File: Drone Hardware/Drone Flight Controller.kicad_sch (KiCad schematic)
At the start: 51 parts, among them J1 USB_B_Micro, J10 UART6_RX, J11 SDA_PAD, J12 PPM_IN, J13 UART3_TX, J14 UART3_RX, J15 Pad, J2 S4, J3 S1, J4 UART1_TX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

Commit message: Basic PCB outline created
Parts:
- SW1: footprint (none) -> Button_Switch_SMD:SW_DIP_SPSTx01_Slide_Copal_CVS-01xB_W5.9mm_P1mm
- Y1: footprint (none) -> Crystal:Crystal_SMD_3225-4Pin_3.2x2.5mm
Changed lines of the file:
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@@
     (property "Reference" "Y1" (id 0) (at 148.59 80.01 0))
     (property "Value" "8MHz" (id 1) (at 149.86 90.17 0))
-    (property "Footprint" "" (id 2) (at 146.05 85.09 0)
+    (property "Footprint" "Crystal:Crystal_SMD_3225-4Pin_3.2x2.5mm" (id 2) (at 146.05 85.09 0)
       (effects (font (size 1.27 1.27)) hide)
     )
@@
     (property "Reference" "SW1" (id 0) (at 148.59 54.61 0))
     (property "Value" "SW_SPDT" (id 1) (at 148.59 62.23 0))
-    (property "Footprint" "" (id 2) (at 147.32 57.15 0)
+    (property "Footprint" "Button_Switch_SMD:SW_DIP_SPSTx01_Slide_Copal_CVS-01xB_W5.9mm_P1mm" (id 2) (at 147.32 57.15 0)
       (effects (font (size 1.27 1.27)) hide)
     )
@@
     )
     (path "/f7f7def0-4a30-49f0-a6ee-43201f0a01bb"
-      (reference "SW1") (unit 1) (value "SW_SPDT") (footprint "")
+      (reference "SW1") (unit 1) (value "SW_SPDT") (footprint "Button_Switch_SMD:SW_DIP_SPSTx01_Slide_Copal_CVS-01xB_W5.9mm_P1mm")
     )
     (path "/da8d870f-60bd-4388-b575-5bfb17f73489"
@@
     )
     (path "/d088e369-8987-468f-b0cd-47a0a3df6e73"
-      (reference "Y1") (unit 1) (value "8MHz") (footprint "")
-    )
-  )
+      (reference "Y1") (unit 1) (value "8MHz") (footprint "Crystal:Crystal_SMD_3225-4Pin_3.2x2.5mm")
+    )
+  )

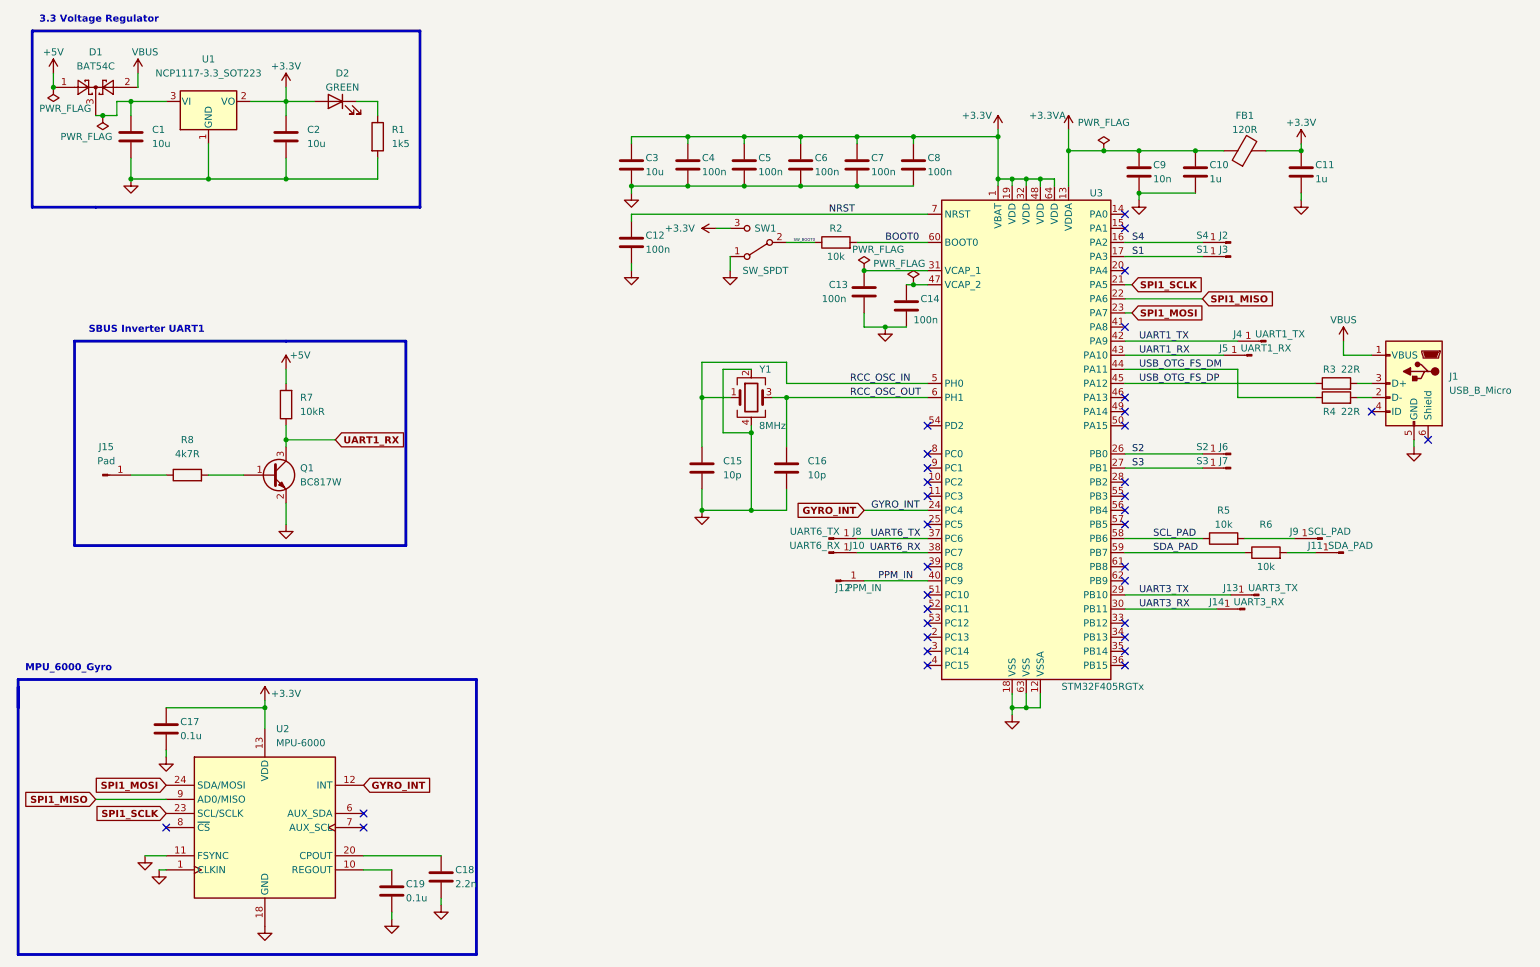
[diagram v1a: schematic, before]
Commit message: Wired the decoupling capacitors, crystal and USB
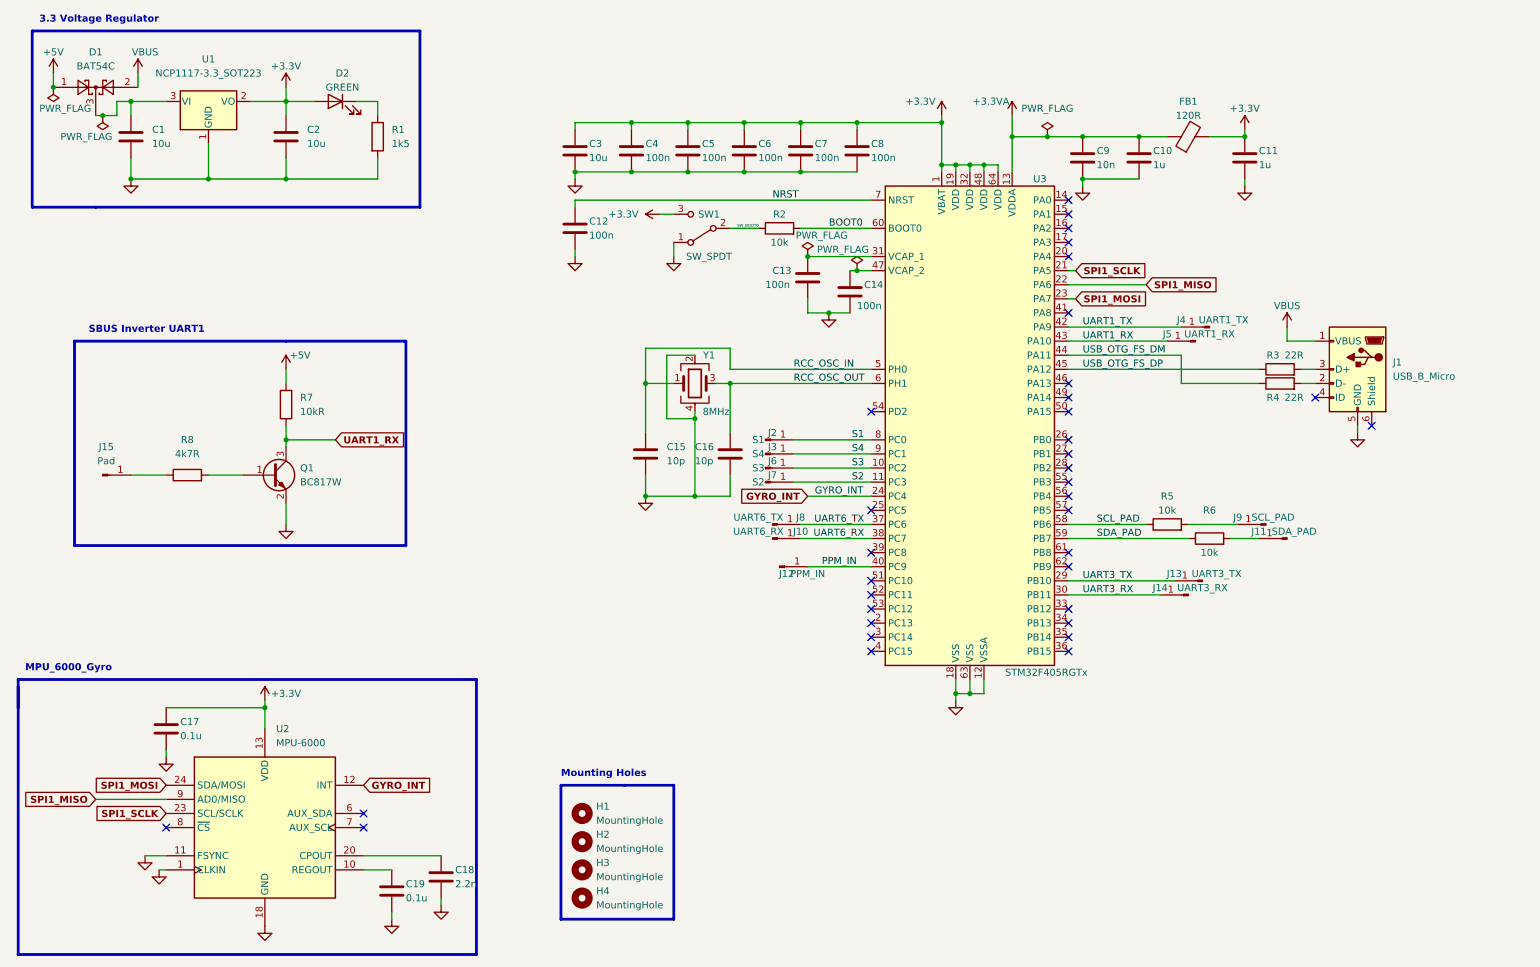
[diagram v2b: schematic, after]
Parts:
- added H1, H2, H3, H4: MountingHole, MountingHole:MountingHole_2.2mm_M2, symbol Mechanical:MountingHole
- J2: value S4 -> S1; footprint Connector_Wire:SolderWirePad_1x01_SMD_5x10mm -> Connector_Wire:SolderWirePad_1x01_SMD_1x2mm
- J3: value S1 -> S4; footprint Connector_Wire:SolderWirePad_1x01_SMD_5x10mm -> Connector_Wire:SolderWirePad_1x01_SMD_1x2mm
- J6: value S2 -> S3; footprint Connector_Wire:SolderWirePad_1x01_SMD_5x10mm -> Connector_Wire:SolderWirePad_1x01_SMD_1x2mm
- J7: value S3 -> S2; footprint Connector_Wire:SolderWirePad_1x01_SMD_5x10mm -> Connector_Wire:SolderWirePad_1x01_SMD_1x2mm
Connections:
- net S1: now also J2.1 (Pin_1), U3.8 (PC0); no longer J3.1 (Pin_1), U3.17 (PA3)
- net S2: now also J7.1 (Pin_1), U3.11 (PC3); no longer J6.1 (Pin_1), U3.26 (PB0)
- net S3: now also J6.1 (Pin_1), U3.10 (PC2); no longer J7.1 (Pin_1), U3.27 (PB1)
- net S4: now also J3.1 (Pin_1), U3.9 (PC1); no longer J2.1 (Pin_1), U3.16 (PA2)
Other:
- note added: "Mounting Holes"
- moved on the sheet: C10, C11, C12, C13, C14, C15, C16, C3, C4, C5, C6, C7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

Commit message: Reconfigured linux repository and finished version 1.0 of the flight controller.
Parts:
- removed J15: Pad, Connector_Wire:SolderWirePad_1x01_SMD_1x2mm, symbol Connector:Conn_01x01_Male
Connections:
- net +5V: now also C1.1, D1.3, U1.3 (VI); no longer D1.1
- net at R8.1: now also J5.1 (Pin_1)
- net UART1_RX renamed UART1_RX_OUT
- net UART1_RX_OUT: no longer J5.1 (Pin_1)
- new net VDD: D1.1
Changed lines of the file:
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@@
   (junction (at 62.23 92.71) (diameter 0) (color 0 0 0 0)
+  )
+  (junction (at 27.94 34.29) (diameter 0) (color 0 0 0 0)
   )
   (junction (at 124.46 35.56) (diameter 0) (color 0 0 0 0)
@@
     (stroke (width 0) (type default) (color 0 0 0 0))
   )
+  (wire (pts (xy 20.32 35.56) (xy 27.94 35.56))
+    (stroke (width 0) (type default) (color 0 0 0 0))
+  )
   (wire (pts (xy 185.42 43.18) (xy 185.42 44.45))
     (stroke (width 0) (type default) (color 0 0 0 0))
@@
     (stroke (width 0.5) (type solid) (color 0 0 0 0))
   )
-  (wire (pts (xy 62.23 92.71) (xy 71.12 92.71))
+  (wire (pts (xy 62.23 92.71) (xy 66.04 92.71))
     (stroke (width 0) (type default) (color 0 0 0 0))
   )
@@
     (stroke (width 0) (type default) (color 0 0 0 0))
   )
+  (wire (pts (xy 203.2 74.93) (xy 222.25 74.93))
+    (stroke (width 0) (type default) (color 0 0 0 0))
+  )
   (wire (pts (xy 156.21 59.69) (xy 167.64 59.69))
     (stroke (width 0) (type default) (color 0 0 0 0))
@@
     (stroke (width 0) (type default) (color 0 0 0 0))
   )
-  (wire (pts (xy 34.29 99.06) (xy 40.64 99.06))
+  (wire (pts (xy 39.37 99.06) (xy 40.64 99.06))
     (stroke (width 0) (type default) (color 0 0 0 0))
   )
@@
     (stroke (width 0.5) (type solid) (color 0 0 0 0))
   )
-  (wire (pts (xy 203.2 74.93) (xy 220.98 74.93))
-    (stroke (width 0) (type default) (color 0 0 0 0))
-  )
   (wire (pts (xy 180.34 34.29) (xy 180.34 35.56))
     (stroke (width 0) (type default) (color 0 0 0 0))
@@
   )
   (wire (pts (xy 114.3 35.56) (xy 124.46 35.56))
+    (stroke (width 0) (type default) (color 0 0 0 0))
+  )
+  (wire (pts (xy 27.94 35.56) (xy 27.94 34.29))
     (stroke (width 0) (type default) (color 0 0 0 0))
   )
@@
     )
   )
-  (global_label "UART1_RX" (shape input) (at 71.12 92.71 0) (fields_autoplaced)
+  (global_label "UART1_RX_OUT" (shape input) (at 66.04 92.71 0) (fields_autoplaced)
     (effects (font (size 1.27 1.27) bold) (justify left))
-    (property "Intersheet References" "${INTERSHEET_REFS}" (id 0) (at 83.0368 92.583 0)
+    (property "Intersheet References" "${INTERSHEET_REFS}" (id 0) (at 82.553 92.583 0)
+      (effects (font (size 1.27 1.27) bold) (justify left) hide)
+    )
+  )
+  (global_label "UART1_RX_OUT" (shape input) (at 222.25 74.93 0) (fields_autoplaced)
+    (effects (font (size 1.27 1.27) bold) (justify left))
+    (property "Intersheet References" "${INTERSHEET_REFS}" (id 0) (at 238.763 74.803 0)
       (effects (font (size 1.27 1.27) bold) (justify left) hide)
     )
@@
     (pin "2")
   )
+  (symbol (lib_id "power:VDD") (at 20.32 26.67 0) (unit 1)
+    (in_bom yes) (on_board yes)
+    (property "Reference" "#PWR0102" (id 0) (at 20.32 30.48 0)
+      (effects (font (size 1.27 1.27)) hide)
+    )
+    (property "Value" "VDD" (id 1) (at 20.32 22.86 0))
+    (property "Footprint" "" (id 2) (at 20.32 26.67 0)
+      (effects (font (size 1.27 1.27)) hide)
+    )
+    (property "Datasheet" "" (id 3) (at 20.32 26.67 0)
+      (effects (font (size 1.27 1.27)) hide)
+    )
+    (pin "1")
+  )
   (symbol (lib_id "Device:C") (at 144.78 40.64 0) (unit 1)
     (in_bom yes) (on_board yes)
@@
     )
     (property "Datasheet" "" (id 3) (at 81.28 179.07 0)
-      (effects (font (size 1.27 1.27)) hide)
-    )
-    (pin "1")
-  )
-  (symbol (lib_id "power:+5V") (at 20.32 26.67 0) (unit 1)
-    (in_bom yes) (on_board yes)
-    (property "Reference" "#PWR01" (id 0) (at 20.32 30.48 0)
-      (effects (font (size 1.27 1.27)) hide)
-    )
-    (property "Value" "+5V" (id 1) (at 20.32 22.86 0))
-    (property "Footprint" "" (id 2) (at 20.32 26.67 0)
-      (effects (font (size 1.27 1.27)) hide)
-    )
-    (property "Datasheet" "" (id 3) (at 20.32 26.67 0)
       (effects (font (size 1.27 1.27)) hide)
     )
@@
     (pin "1")
   )
+  (symbol (lib_id "Connector:Conn_01x01_Male") (at 34.29 99.06 0) (unit 1)
+    (in_bom yes) (on_board yes)
+    (property "Reference" "J5" (id 0) (at 39.37 100.33 0))
+    (property "Value" "UART1_RX" (id 1) (at 31.75 100.33 0))
+    (property "Footprint" "Connector_Wire:SolderWirePad_1x01_SMD_1x2mm" (id 2) (at 34.29 99.06 0)
+      (effects (font (size 1.27 1.27)) hide)
+    )
+    (property "Datasheet" "~" (id 3) (at 34.29 99.06 0)
+      (effects (font (size 1.27 1.27)) hide)
+    )
+    (pin "1")
+  )
   (symbol (lib_id "Connector:Conn_01x01_Male") (at 149.86 110.49 0) (unit 1)
     (in_bom yes) (on_board yes)
@@
     )
     (property "Datasheet" "~" (id 3) (at 224.79 120.65 0)
+      (effects (font (size 1.27 1.27)) hide)
+    )
+    (pin "1")
+  )
+  (symbol (lib_id "power:+5V") (at 20.32 35.56 180) (unit 1)
+    (in_bom yes) (on_board yes) (fields_autoplaced)
+    (property "Reference" "#PWR?" (id 0) (at 20.32 31.75 0)
+      (effects (font (size 1.27 1.27)) hide)
+    )
+    (property "Value" "+5V" (id 1) (at 20.32 40.64 0))
+    (property "Footprint" "" (id 2) (at 20.32 35.56 0)
+      (effects (font (size 1.27 1.27)) hide)
+    )
+    (property "Datasheet" "" (id 3) (at 20.32 35.56 0)
       (effects (font (size 1.27 1.27)) hide)
     )
@@
     (pin "1")
   )
-  (symbol (lib_id "Connector:Conn_01x01_Male") (at 226.06 74.93 180) (unit 1)
-    (in_bom yes) (on_board yes)
-    (property "Reference" "J5" (id 0) (at 220.98 73.66 0))
-    (property "Value" "UART1_RX" (id 1) (at 228.6 73.66 0))
-    (property "Footprint" "Connector_Wire:SolderWirePad_1x01_SMD_1x2mm" (id 2) (at 226.06 74.93 0)
-      (effects (font (size 1.27 1.27)) hide)
-    )
-    (property "Datasheet" "~" (id 3) (at 226.06 74.93 0)
-      (effects (font (size 1.27 1.27)) hide)
-    )
-    (pin "1")
-  )
   (symbol (lib_id "Device:R") (at 228.6 110.49 90) (unit 1)
     (in_bom yes) (on_board yes)
@@
     (pin "2")
   )
-  (symbol (lib_id "Connector:Conn_01x01_Male") (at 29.21 99.06 0) (unit 1)
-    (in_bom yes) (on_board yes) (fields_autoplaced)
-    (property "Reference" "J15" (id 0) (at 29.845 93.98 0))
-    (property "Value" "Pad" (id 1) (at 29.845 96.52 0))
-    (property "Footprint" "Connector_Wire:SolderWirePad_1x01_SMD_1x2mm" (id 2) (at 29.21 99.06 0)
-      (effects (font (size 1.27 1.27)) hide)
-    )
-    (property "Datasheet" "~" (id 3) (at 29.21 99.06 0)
-      (effects (font (size 1.27 1.27)) hide)
-    )
-    (pin "1")
-  )
   (symbol (lib_id "Device:C") (at 205.74 41.91 0) (unit 1)
     (in_bom yes) (on_board yes)
@@
       (reference "#FLG0105") (unit 1) (value "PWR_FLAG") (footprint "")
     )
-    (path "/7263bf79-048b-4792-ab1b-2036a6e2abc3"
-      (reference "#PWR01") (unit 1) (value "+5V") (footprint "")
-    )
     (path "/564c888e-7f06-4e73-bff8-adcbfb4fd709"
       (reference "#PWR02") (unit 1) (value "VBUS") (footprint "")
@@
       (reference "#PWR0101") (unit 1) (value "GND") (footprint "")
     )
+    (path "/1d45b3ce-879f-4273-bf8b-ebe1b0d75768"
+      (reference "#PWR0102") (unit 1) (value "VDD") (footprint "")
+    )
+    (path "/930876d7-acf1-445f-acf9-f2f68e31b539"
+      (reference "#PWR?") (unit 1) (value "+5V") (footprint "")
+    )
     (path "/add27d77-588e-4e90-a703-0ea61c75253d"
       (reference "C1") (unit 1) (value "10u") (footprint "Capacitor_SMD:C_0805_2012Metric")
@@
       (reference "J4") (unit 1) (value "UART1_TX") (footprint "Connector_Wire:SolderWirePad_1x01_SMD_1x2mm")
     )
-    (path "/ead95198-0587-4851-bde0-5cc3de6b2110"
+    (path "/8bb131ba-d58c-43be-a5f3-2a6efab7a252"
       (reference "J5") (unit 1) (value "UART1_RX") (footprint "Connector_Wire:SolderWirePad_1x01_SMD_1x2mm")
     )
@@
       (reference "J14") (unit 1) (value "UART3_RX") (footprint "Connector_Wire:SolderWirePad_1x01_SMD_1x2mm")
     )
-    (path "/f138238c-e1ee-450d-b4bb-bc8a8423972e"
-      (reference "J15") (unit 1) (value "Pad") (footprint "Connector_Wire:SolderWirePad_1x01_SMD_1x2mm")
-    )
     (path "/27abf5fc-ba91-4fb5-b084-5eae5121c946"
